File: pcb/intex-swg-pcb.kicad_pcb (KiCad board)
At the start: 2 copper layers, 70.2 x 90 mm, 14 parts, among them J1 230V, J2 Relay Board, J3 Display Board, J4 Main Board, J5 5V Pin Sel, J6 GND Pin Sel

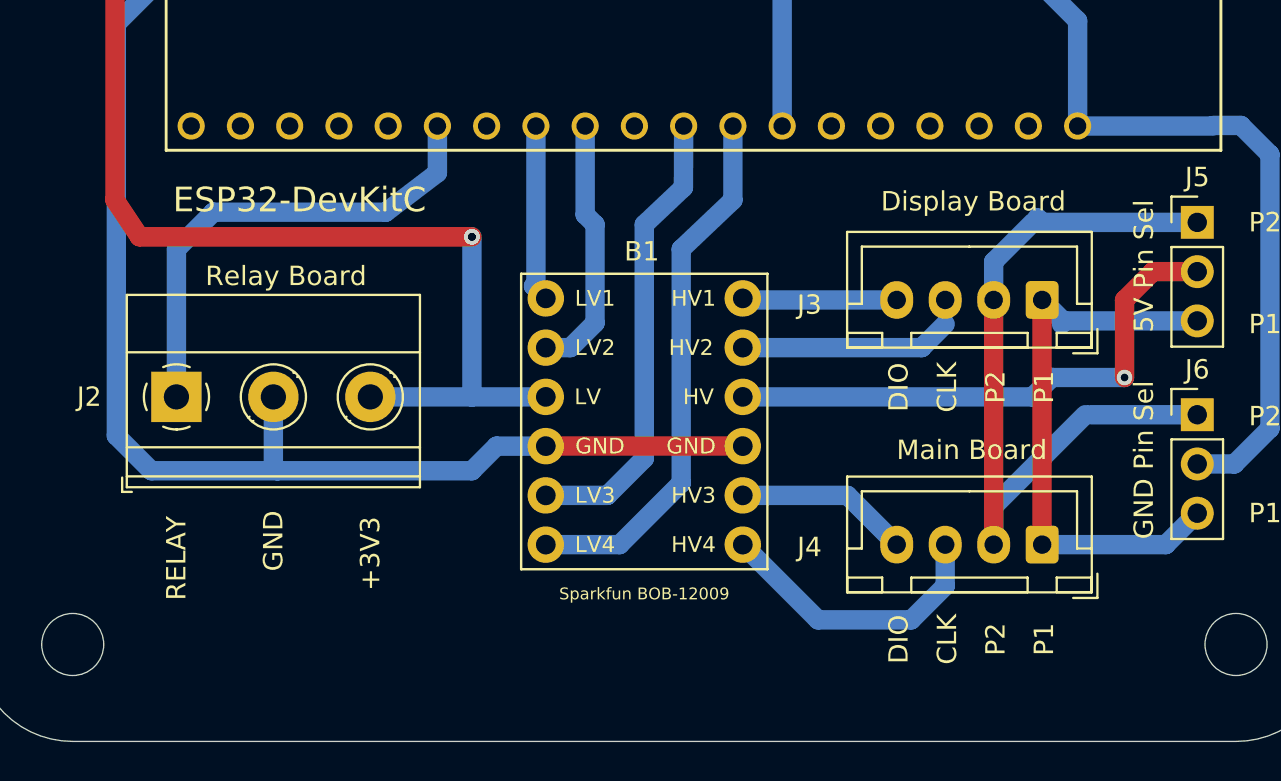
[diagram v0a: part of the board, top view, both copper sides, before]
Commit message: Swapped relay to GPIO2
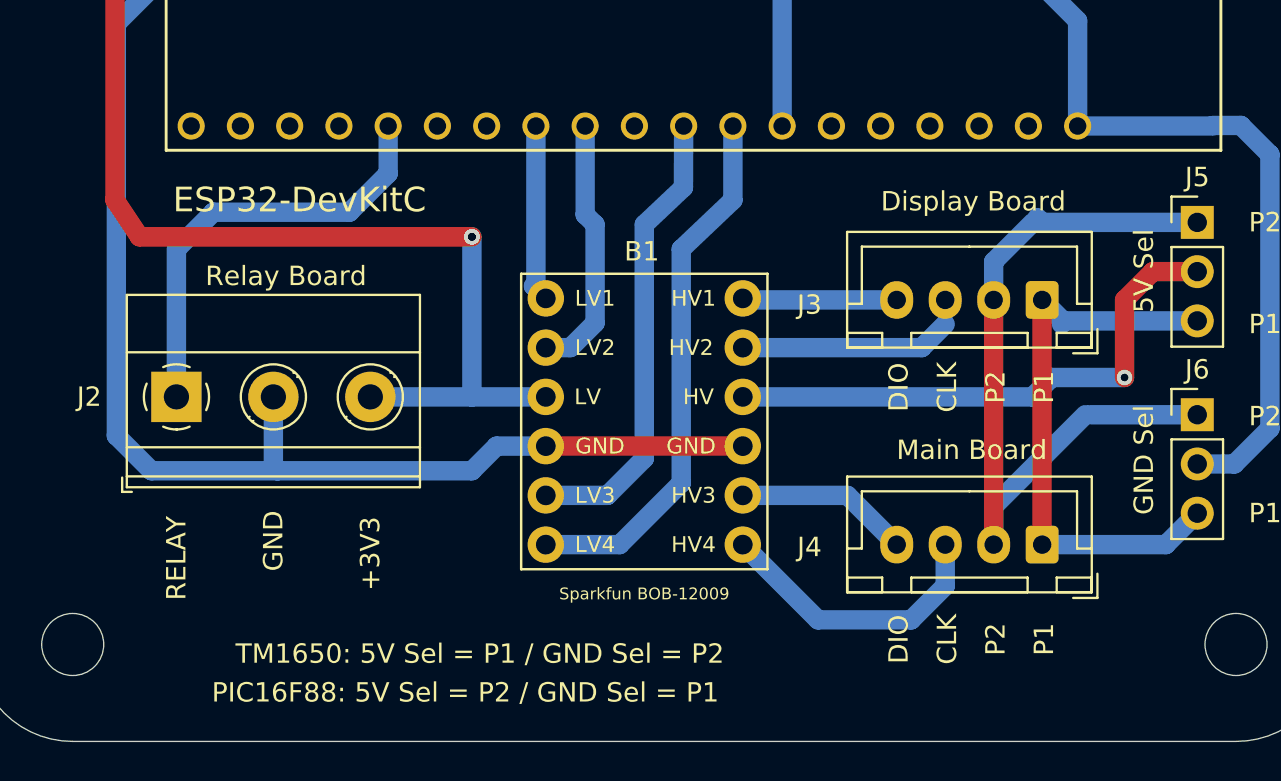
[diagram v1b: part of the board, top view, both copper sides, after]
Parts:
- J5: value 5V Pin Sel -> 5V_INTEX Pin Select
- J6: value GND Pin Sel -> GND Pin Select
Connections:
- MD1 pad 24: Net-(MD1-Pad24) -> /RELAY
- MD1 pad 25: /RELAY -> Net-(MD1-Pad25)
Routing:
- net /RELAY: track 25.0 -> 22.6 mm
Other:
- board text added: "PIC16F88: 5V Sel = P2 / GND Sel = P1"
- board text added: "TM1650: 5V Sel = P1 / GND Sel = P2"

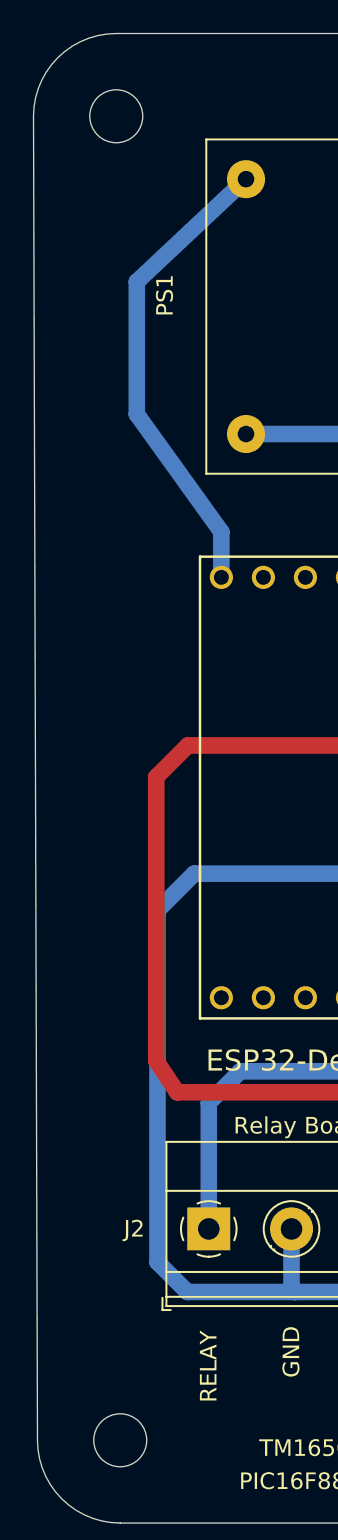
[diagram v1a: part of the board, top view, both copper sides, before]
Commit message: Corrected top left mounting hole, that was 0.24mm offset
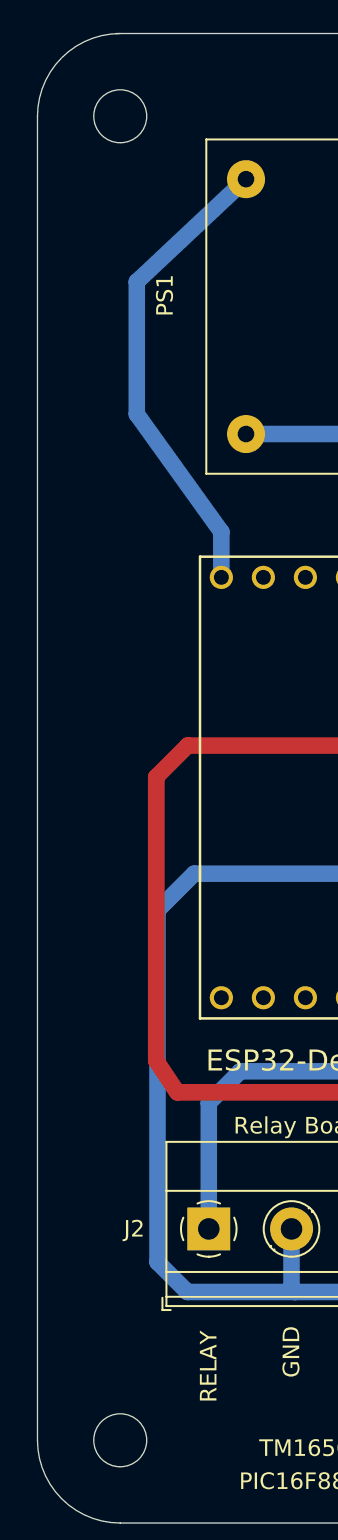
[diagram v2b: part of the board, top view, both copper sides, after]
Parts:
- moved REF** 0.24 mm to (102.6, 56.5)
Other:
- board size 70.2 x 90 mm -> 70 x 90 mm
